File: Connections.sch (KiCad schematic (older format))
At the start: 18 parts, among them P4 CONN_02X07, P6 CONN_02X07, P7 CONN_02X07, P8 CONN_02X07, SW1 SW_PUSH, SW2 SW_PUSH

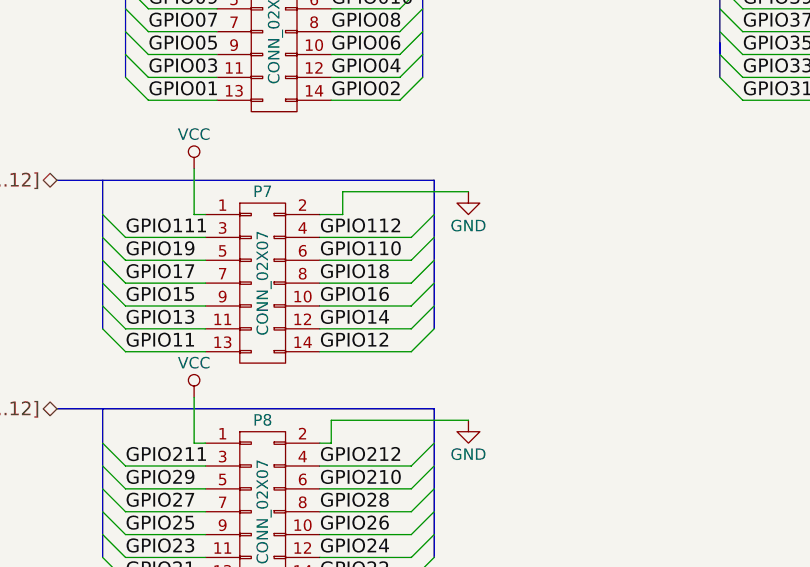
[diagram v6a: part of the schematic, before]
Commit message: Changed SPI Connection to support Multi-Master
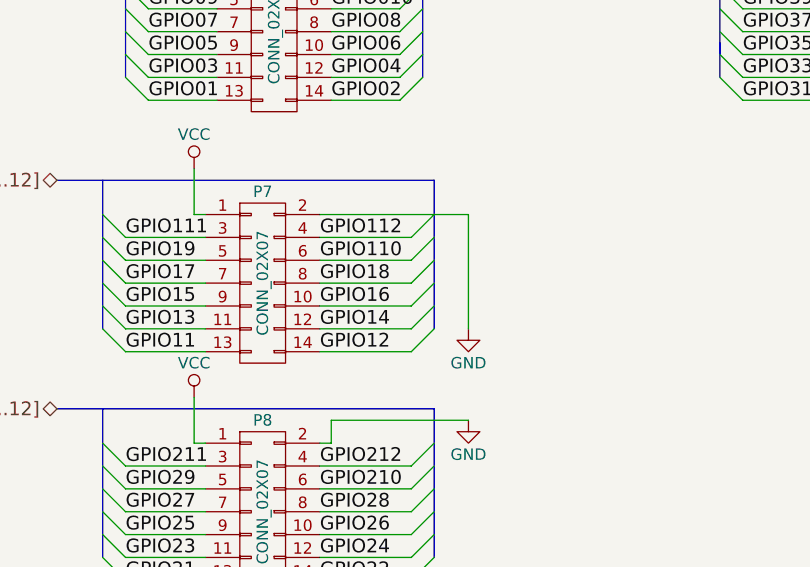
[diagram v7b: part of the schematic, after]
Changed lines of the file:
@@
 $EndComp
 $Comp
-L GND #PWR037
+L GND #PWR044
 U 1 1 5782F652
 P 4450 2300
-F 0 "#PWR037" H 4450 2050 50  0001 C CNN
+F 0 "#PWR044" H 4450 2050 50  0001 C CNN
 F 1 "GND" H 4450 2150 50  0000 C CNN
 F 2 "" H 4450 2300 50  0000 C CNN
@@
 LED3
 $Comp
-L GND #PWR038
+L GND #PWR045
 U 1 1 5782FC2F
 P 7500 2250
-F 0 "#PWR038" H 7500 2000 50  0001 C CNN
+F 0 "#PWR045" H 7500 2000 50  0001 C CNN
 F 1 "GND" H 7500 2100 50  0000 C CNN
 F 2 "" H 7500 2250 50  0000 C CNN
@@
 GPIO0[1..12]
 $Comp
-L GND #PWR039
+L GND #PWR046
 U 1 1 5784BCA2
 P 4650 3450
-F 0 "#PWR039" H 4650 3200 50  0001 C CNN
+F 0 "#PWR046" H 4650 3200 50  0001 C CNN
 F 1 "GND" H 4650 3300 50  0000 C CNN
 F 2 "" H 4650 3450 50  0000 C CNN
@@
 GPIO1[1..12]
 $Comp
-L GND #PWR040
+L GND #PWR047
 U 1 1 5785BA09
-P 4750 4550
-F 0 "#PWR040" H 4750 4300 50  0001 C CNN
-F 1 "GND" H 4750 4400 50  0000 C CNN
-F 2 "" H 4750 4550 50  0000 C CNN
-F 3 "" H 4750 4550 50  0000 C CNN
-	1    4750 4550
+P 4750 5150
+F 0 "#PWR047" H 4750 4900 50  0001 C CNN
+F 1 "GND" H 4750 5000 50  0000 C CNN
+F 2 "" H 4750 5150 50  0000 C CNN
+F 3 "" H 4750 5150 50  0000 C CNN
+	1    4750 5150
 	1    0    0    -1
 $EndComp
@@
 GPIO2[1..12]
 $Comp
-L GND #PWR041
+L GND #PWR048
 U 1 1 5785C545
 P 4750 5550
-F 0 "#PWR041" H 4750 5300 50  0001 C CNN
+F 0 "#PWR048" H 4750 5300 50  0001 C CNN
 F 1 "GND" H 4750 5400 50  0000 C CNN
 F 2 "" H 4750 5550 50  0000 C CNN
@@
 GPIO36
 $Comp
-L GND #PWR042
+L GND #PWR049
 U 1 1 57864245
 P 7400 3450
-F 0 "#PWR042" H 7400 3200 50  0001 C CNN
+F 0 "#PWR049" H 7400 3200 50  0001 C CNN
 F 1 "GND" H 7400 3300 50  0000 C CNN
 F 2 "" H 7400 3450 50  0000 C CNN
@@
 $EndComp
 $Comp
-L VCC #PWR043
+L VCC #PWR050
 U 1 1 57871160
 P 3550 3350
-F 0 "#PWR043" H 3550 3200 50  0001 C CNN
+F 0 "#PWR050" H 3550 3200 50  0001 C CNN
 F 1 "VCC" H 3550 3500 50  0000 C CNN
 F 2 "" H 3550 3350 50  0000 C CNN
@@
 $EndComp
 $Comp
-L VCC #PWR044
+L VCC #PWR051
 U 1 1 578714DD
 P 6300 3250
-F 0 "#PWR044" H 6300 3100 50  0001 C CNN
+F 0 "#PWR051" H 6300 3100 50  0001 C CNN
 F 1 "VCC" H 6300 3400 50  0000 C CNN
 F 2 "" H 6300 3250 50  0000 C CNN
@@
 $EndComp
 $Comp
-L VCC #PWR045
+L VCC #PWR052
 U 1 1 57871512
 P 3550 4450
-F 0 "#PWR045" H 3550 4300 50  0001 C CNN
+F 0 "#PWR052" H 3550 4300 50  0001 C CNN
 F 1 "VCC" H 3550 4600 50  0000 C CNN
 F 2 "" H 3550 4450 50  0000 C CNN
@@
 $EndComp
 $Comp
-L VCC #PWR046
+L VCC #PWR053
 U 1 1 57871547
 P 3550 5450
-F 0 "#PWR046" H 3550 5300 50  0001 C CNN
+F 0 "#PWR053" H 3550 5300 50  0001 C CNN
 F 1 "VCC" H 3550 5600 50  0000 C CNN
 F 2 "" H 3550 5450 50  0000 C CNN
@@
 Wire Wire Line
 	4150 5550 4750 5550
-Wire Wire Line
-	4100 4650 4200 4650
-Wire Wire Line
-	4200 4650 4200 4550
-Wire Wire Line
-	4200 4550 4750 4550
 NoConn ~ 6800 3650
 NoConn ~ 6300 3650
@@
 Connection ~ 6500 2150
 $Comp
-L VCC #PWR047
+L VCC #PWR054
 U 1 1 58AE5184
 P 6400 1250
-F 0 "#PWR047" H 6400 1100 50  0001 C CNN
+F 0 "#PWR054" H 6400 1100 50  0001 C CNN
 F 1 "VCC" H 6400 1400 50  0000 C CNN
 F 2 "" H 6400 1250 50  0000 C CNN
@@
 $EndComp
 $Comp
-L VCC #PWR048
+L VCC #PWR055
 U 1 1 58AE572C
 P 1600 3400
-F 0 "#PWR048" H 1600 3250 50  0001 C CNN
+F 0 "#PWR055" H 1600 3250 50  0001 C CNN
 F 1 "VCC" H 1600 3550 50  0000 C CNN
 F 2 "" H 1600 3400 50  0000 C CNN
@@
 $EndComp
 $Comp
-L GND #PWR049
+L GND #PWR056
 U 1 1 58AE5764
 P 1600 3900
-F 0 "#PWR049" H 1600 3650 50  0001 C CNN
+F 0 "#PWR056" H 1600 3650 50  0001 C CNN
 F 1 "GND" H 1600 3750 50  0000 C CNN
 F 2 "" H 1600 3900 50  0000 C CNN
@@
 Text Notes 1100 3200 0    60   ~ 0
 Nah an Steckerleisten
+Wire Wire Line
+	4100 4650 4750 4650
+Wire Wire Line
+	4750 4650 4750 5150
 $EndSCHEMATC
